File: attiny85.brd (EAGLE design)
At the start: 74.7 x 55.5 mm, 8 parts, among them U1 TINY85-20-DIP

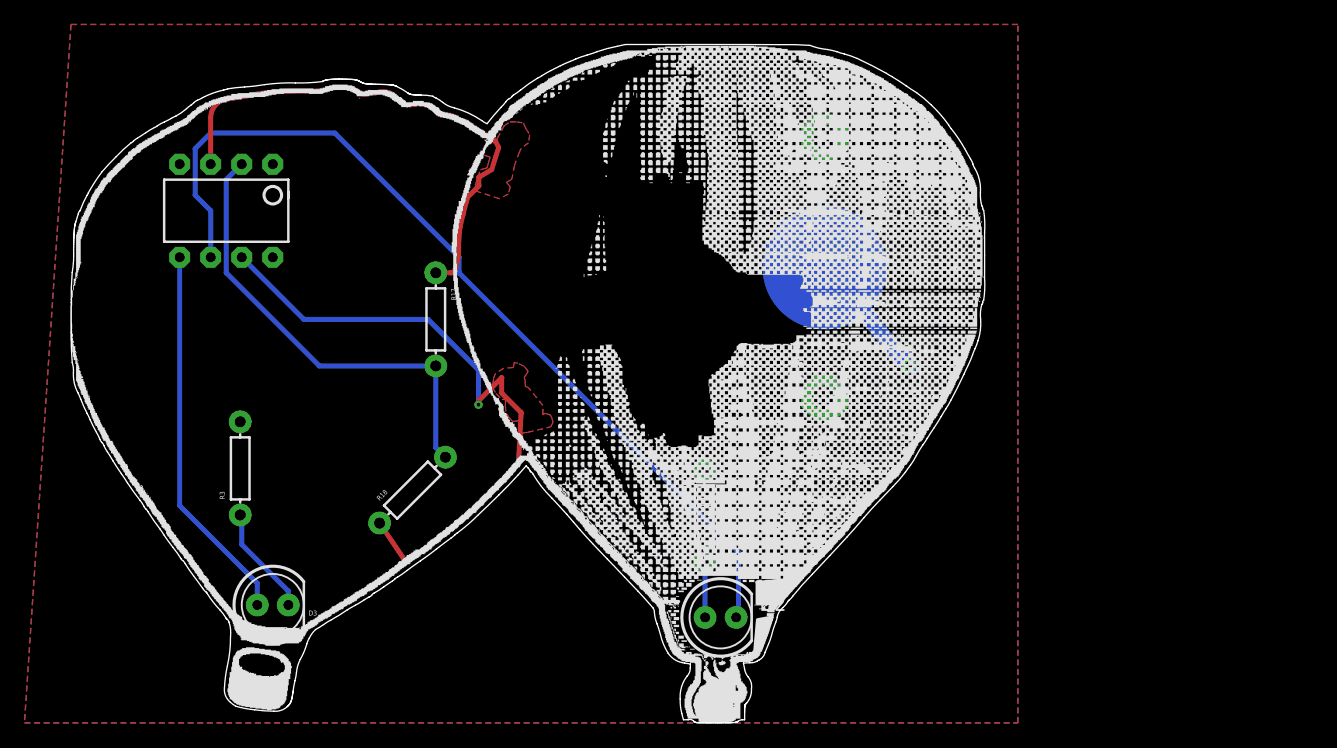
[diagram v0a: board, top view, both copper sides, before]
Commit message: Updated schematic and layout for surface mount components
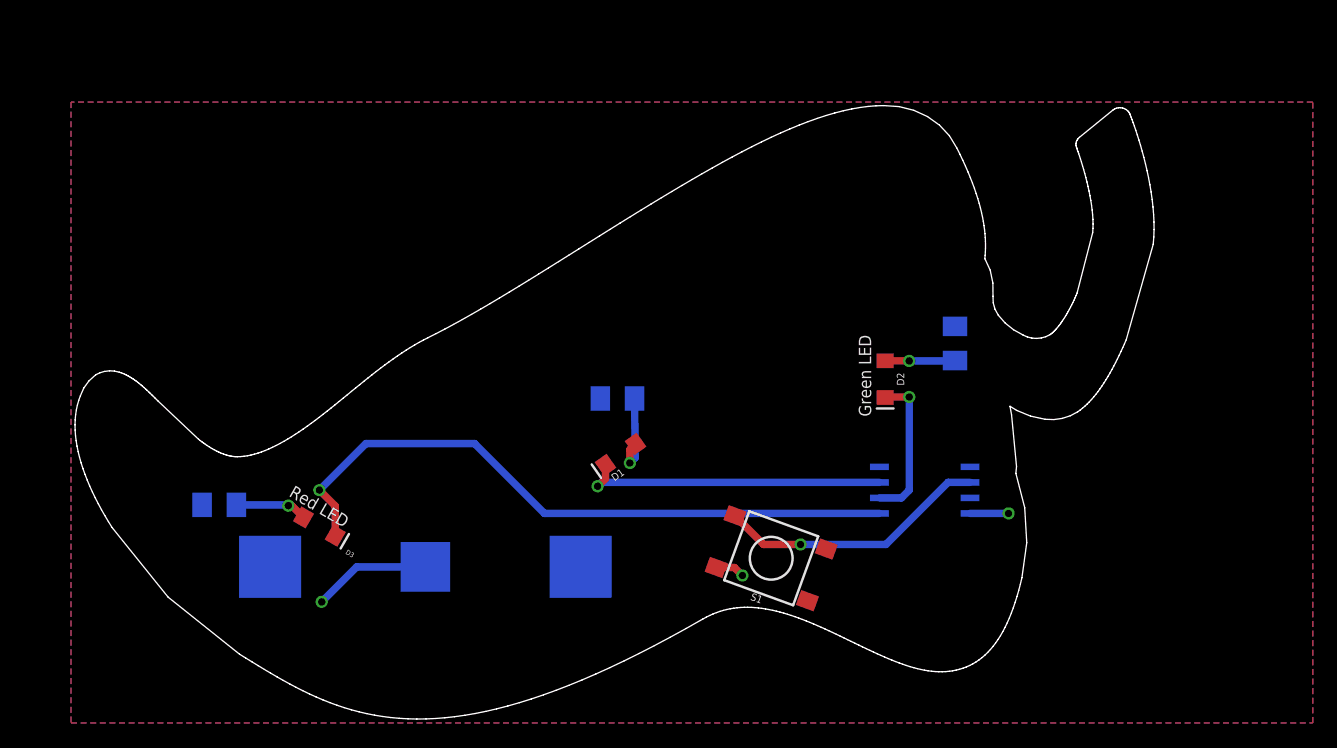
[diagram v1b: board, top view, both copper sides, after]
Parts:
- removed R17, R18: 1M, SparkFun-Resistors:AXIAL-0.3
- removed U1: TINY85-20-DIP, SparkFun-DigitalIC:DIP08
- added D1: (no value), SparkFun-LED:LED-1206
- added R1: 1k, adafruit:M1206
- added S1: MOMENTARY-SWITCH-SPST-SMD-6.2MM-TALL, SparkFun-Switches:TACTILE_SWITCH_SMD_6.2MM_TALL
- added U2: ATTINY85V-10SU, Atmel_By_element14_Batch_1-00:SOIC127P798X216-8N
- BAT1: device adafruit:CR2032-THRU -> adafruit:CR2032-SMD
- D2, D3: device LED:LED5MM -> SparkFun-LED:LED-1206
- R2, R3: device SparkFun-Resistors:AXIAL-0.3 -> adafruit:M1206
- moved BAT1 40.8 mm to (29.0, 12.8), turned to 0 degrees
- moved R2 24.9 mm to (72.3, 31.1), flipped to the bottom
- moved D2 23.7 mm to (66.6, 28.1), turned to 270 degrees
- moved D3 7.46 mm to (20.3, 16.1), turned to 330 degrees
- moved R3 3.44 mm to (12.1, 17.8), flipped to the bottom, turned to 180 degrees
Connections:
- removed net CAP0: R17.P$1, U1.3
- removed net CAP1: R18.P$1, U1.7
- removed net N$20: D2.K, U1.6
- removed net N$9: D3.A, U1.5
- removed net SENSE: R17.P$2, R18.P$2, U1.2
- new net N$1: D3.A, R3.2
- new net N$4: D2.C, U2.6
- new net N$5: D1.A, R1.2
- new net N$6: D1.C, U2.7
- new net N$7: S1.A2, U2.2
- net GND: now also U2.4; no longer R3.P$2, U1.4
- net N$2: now also R2.2; no longer R2.P$2
- net N$3: now also D3.C, U2.5; no longer D3.K, R3.P$1
- net VCC: now also BAT1.+$1, BAT1.+$2, R1.1, R2.1, R3.1, S1.B2, U2.8; no longer BAT1.+1, BAT1.+2, R2.P$1, U1.8
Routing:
- net N$20: track 74.8 -> 0.00 mm
- net CAP1: track 52.8 -> 0.00 mm, vias 1 -> 0
- net N$3: track 9.59 -> 54.0 mm, vias 0 -> 1
- net CAP0: track 42.4 -> 0.00 mm
- net SENSE: track 37.5 -> 0.00 mm
- net N$9: track 31.1 -> 0.00 mm
- net N$6: track 0.00 -> 25.2 mm, vias 0 -> 1
- net N$7: track 0.00 -> 22.3 mm, vias 0 -> 1
- net N$4: track 0.00 -> 12.3 mm, vias 0 -> 1
- net N$5: track 0.00 -> 7.21 mm, vias 0 -> 1
- net N$1: track 0.00 -> 5.92 mm, vias 0 -> 1
- net VCC: track 0.00 -> 2.42 mm, vias 0 -> 1
- net GND: track 10.6 -> 12.8 mm, vias 1 -> 2
- net N$2: track 4.47 -> 5.73 mm, vias 0 -> 1
- removed copper zone on layer 1, net CAP0
- removed copper zone on layer 1, net CAP1
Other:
- board size 74.7 x 55.5 mm -> 88.3 x 50.2 mm
- board text added: "ATTiny85 goes here"
- board text added: "Designed by John 'Warthog9' Hawley For the ABQ MMF Artwork consulted on by Dr. Terri Oda Licensed CC-BY-SA 4.0 2017 http://github.com/warthog9/ABQMMF-Solderkit-2017"
- board text added: "Green LED"
- board text added: "Red LED"
- board text added: "Remember to put some solder here:"
- board text removed: "<-- Put a blob of solder on this pad *BEFORE* the battery holder on"
- board text removed: "Designed by John 'Warthog9' Hawley Licensed CC-BY-SA 4.0 in 2016"
- board text removed: "Remember to program the ATTiny85 *BEFORE* soldering it on"
- board text removed: "Remember to put the components on the other side except for the battery holder"

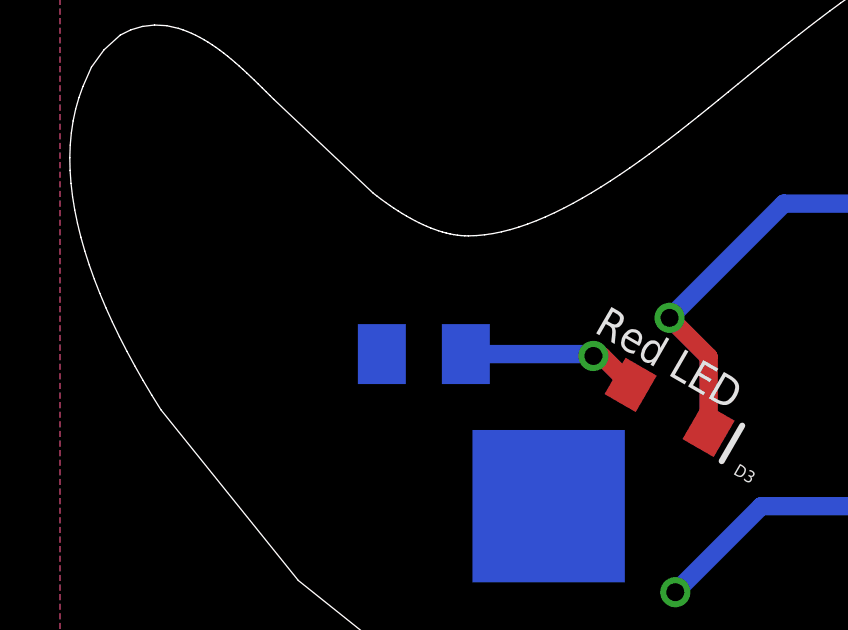
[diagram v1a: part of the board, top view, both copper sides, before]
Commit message: Moving R3 to be more accessible
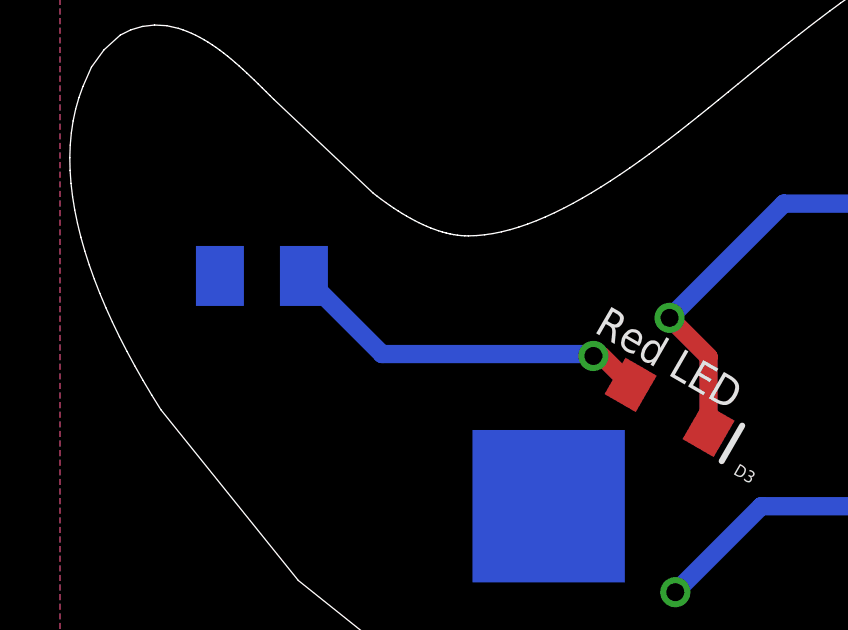
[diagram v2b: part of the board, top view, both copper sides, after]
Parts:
- moved R3 5.99 mm to (6.73, 20.4)
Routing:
- net N$1: track 5.92 -> 12.4 mm
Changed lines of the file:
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@@
 <element name="R2" library="adafruit" package="M1206" value="1k" x="72.3265" y="31.0515" rot="MR270"/>
 <element name="D2" library="SparkFun-LED" package="LED-1206" value="" x="66.6115" y="28.1305" rot="R270"/>
-<element name="R3" library="adafruit" package="M1206" value="1k" x="12.1285" y="17.8435" rot="MR180"/>
+<element name="R3" library="adafruit" package="M1206" value="1k" x="6.731" y="20.447" rot="MR180"/>
 <element name="D3" library="SparkFun-LED" package="LED-1206" value="" x="20.32" y="16.0655" smashed="yes" rot="R330">
 <attribute name="NAME" x="22.41786875" y="13.85710625" size="0.4064" layer="25" ratio="10" rot="R330"/>
@@
 <via x="17.78" y="17.78" extent="1-16" drill="0.6"/>
 <wire x1="17.78" y1="17.78" x2="17.7165" y2="17.8435" width="0.6096" layer="16"/>
-<wire x1="17.7165" y1="17.8435" x2="13.5285" y2="17.8435" width="0.6096" layer="16"/>
+<wire x1="17.7165" y1="17.8435" x2="10.7345" y2="17.8435" width="0.6096" layer="16"/>
+<wire x1="10.7345" y1="17.8435" x2="8.131" y2="20.447" width="0.6096" layer="16"/>
 </signal>
 <signal name="N$3">
